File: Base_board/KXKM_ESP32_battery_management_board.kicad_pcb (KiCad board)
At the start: 4 copper layers, 56.5 x 57.5 mm, 109 parts, among them J1 Conn_01x06, J11 TEST_1P, J13 Wire pad, J14 Wire pad, J15 Wire pad, J16 Wire pad, J2 TEST_1P, J3 Conn_02x10_Odd_Even, J4 Conn_01x04, J5 Conn_01x02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

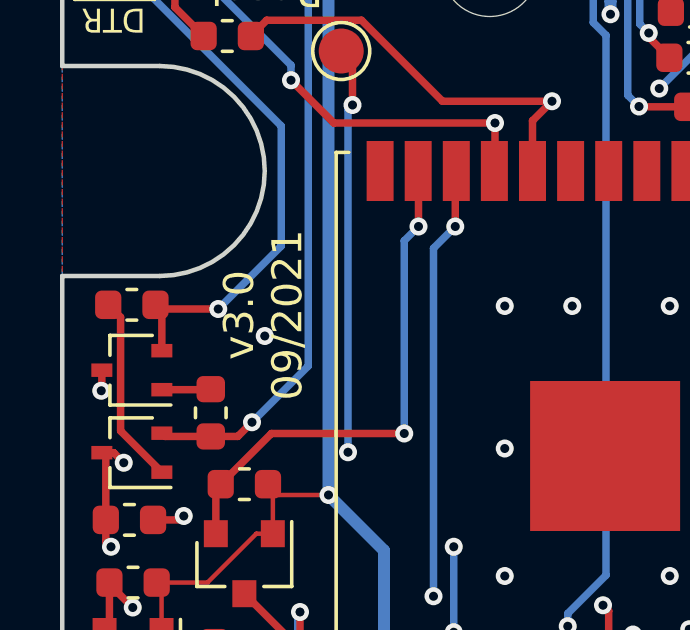
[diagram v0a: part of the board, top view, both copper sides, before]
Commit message: fix silkscreen and version on silk
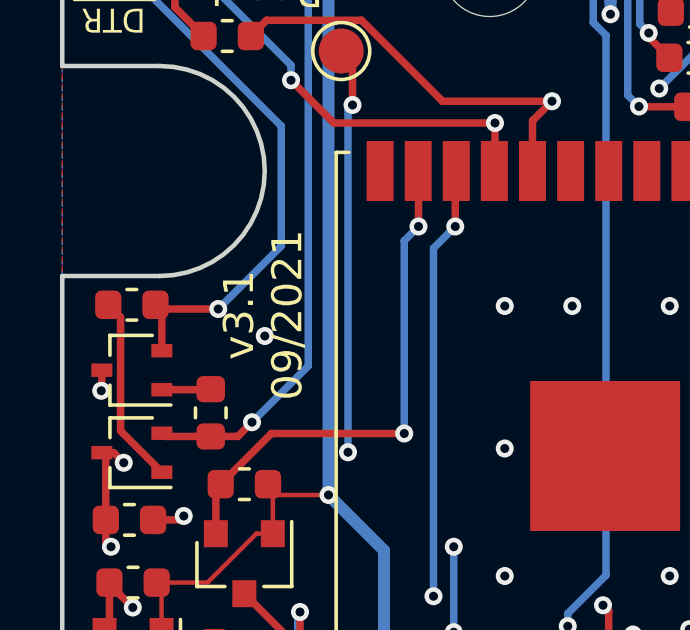
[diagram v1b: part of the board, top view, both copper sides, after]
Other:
- board text added: "V. Henry / Tom Magnier - v3.1 - 09/2021"
- board text added: "v3.1 09/2021"
- board text removed: "V. Henry / Tom Magnier - v3.0 - 09/2021"
- board text removed: "v3.0 09/2021"

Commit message: kicad6
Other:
- net class Default removed
